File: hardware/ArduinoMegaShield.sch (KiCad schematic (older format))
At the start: 26 parts, among them SW101 SW_Coded, SW102 SW_Coded, SW103 SW_Coded, U101 A4988, U102 A4988, U103 A4988

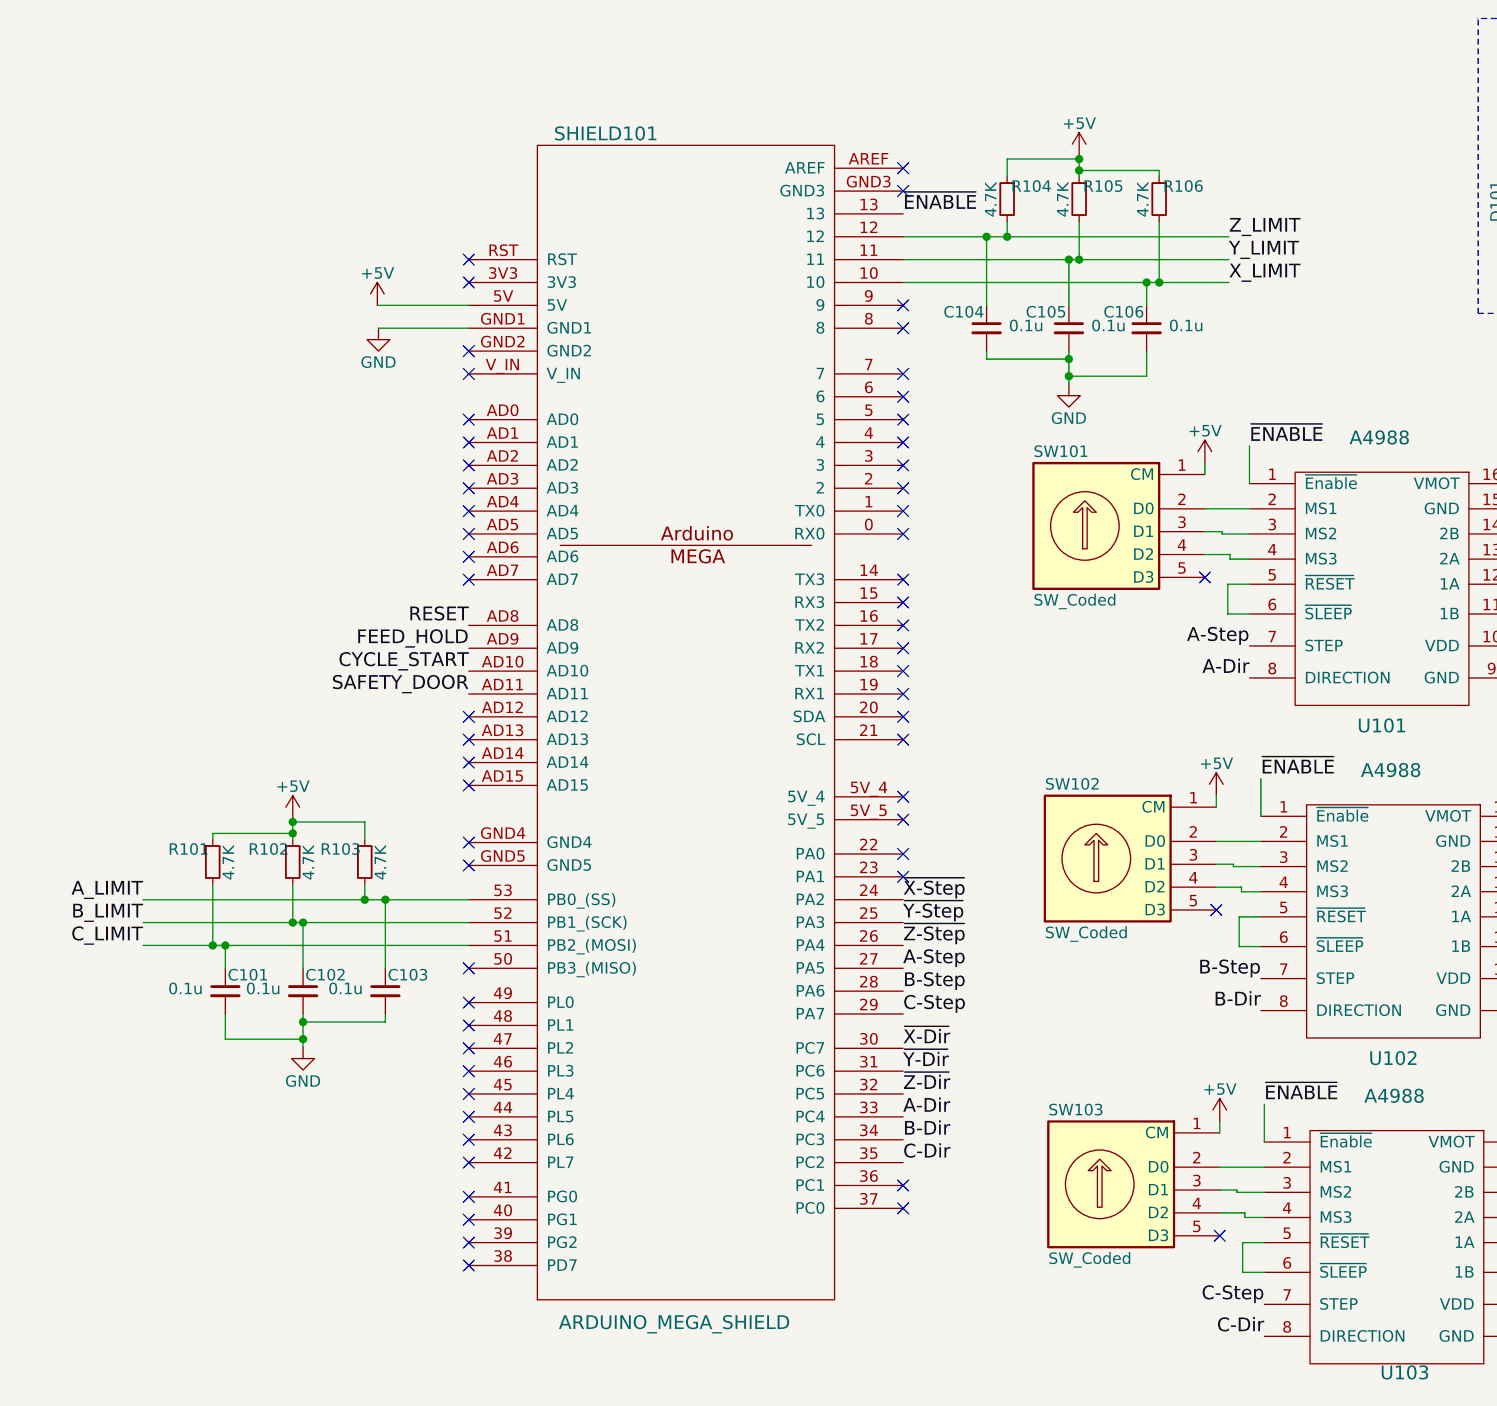
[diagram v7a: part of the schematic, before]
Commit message: changed connector footprints and added rotory dip switch footprint
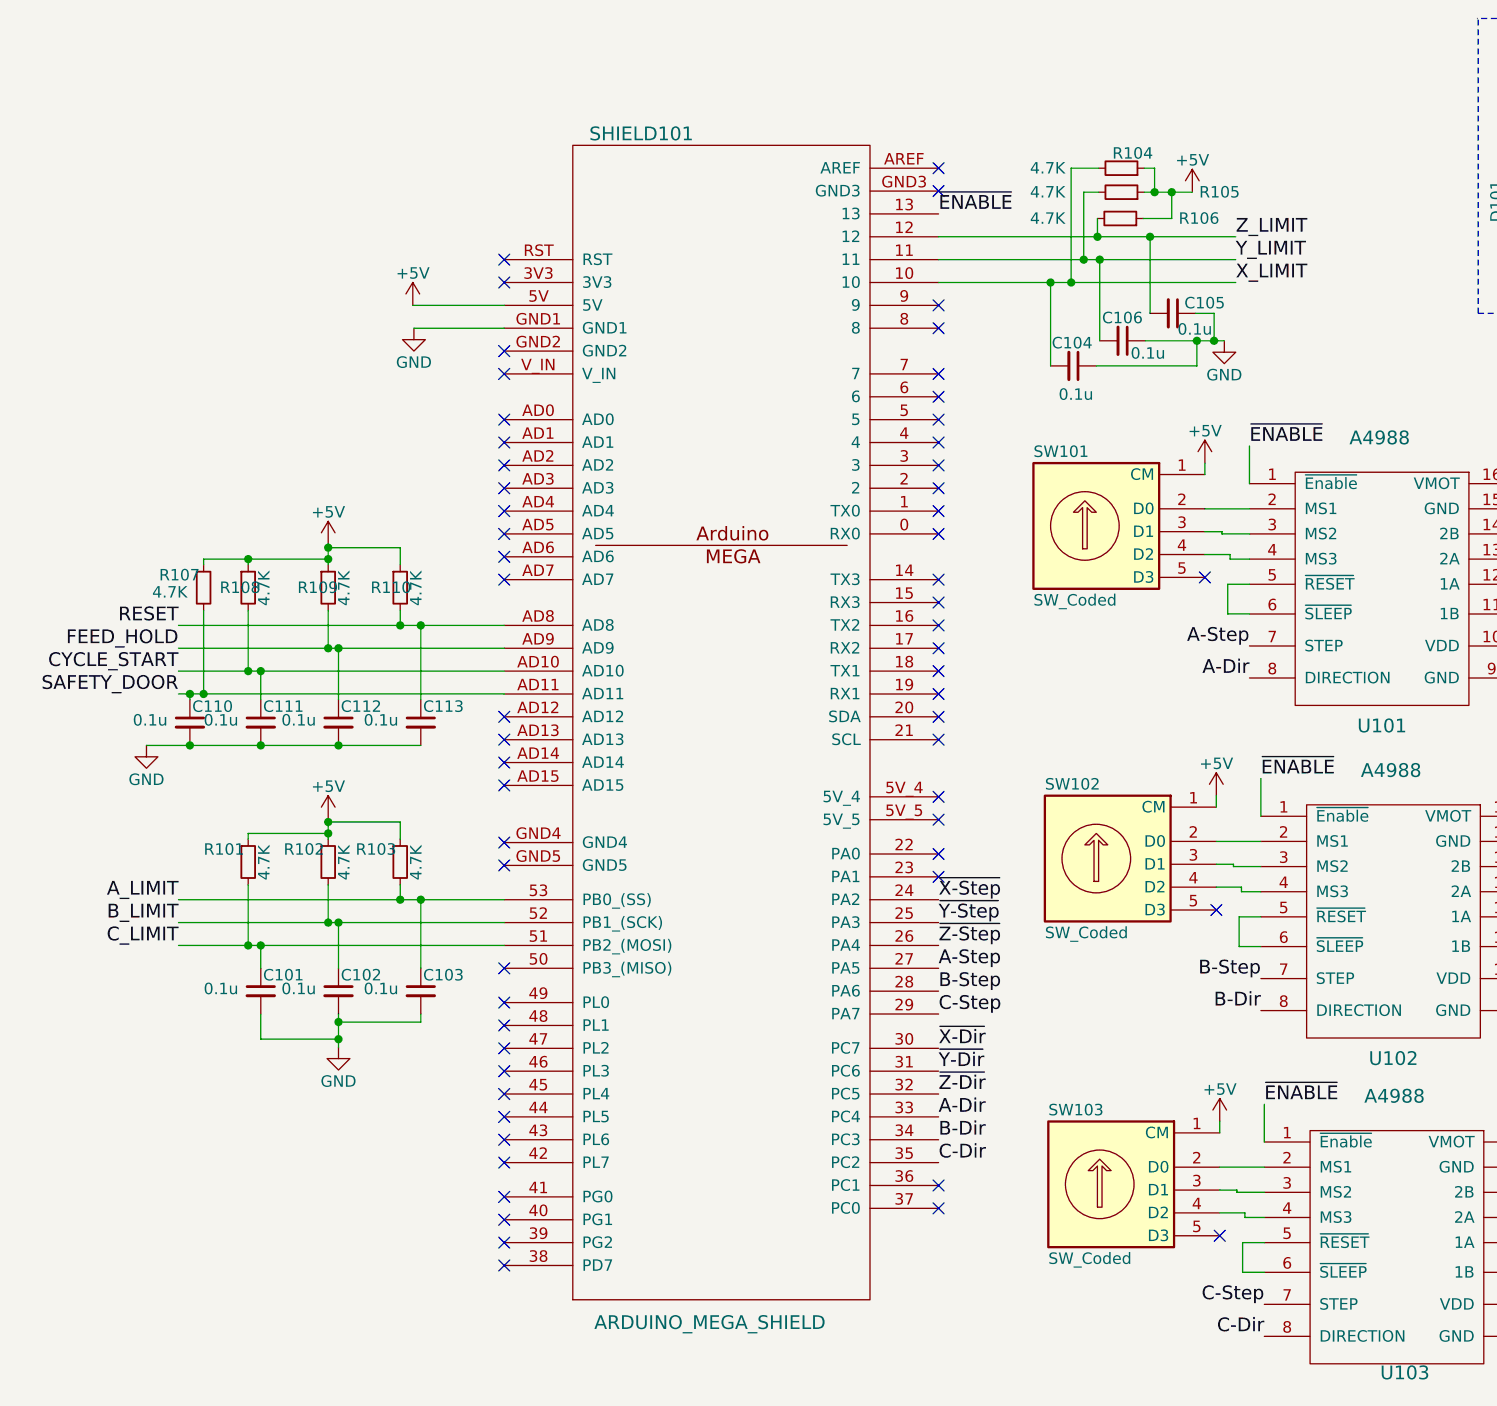
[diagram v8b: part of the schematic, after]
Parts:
- added C110, C111, C112, C113: 0.1u, Capacitors_SMD:C_0805_HandSoldering, symbol C_Small
- added R107, R108, R109, R110: 4.7K, Resistors_SMD:R_0805_HandSoldering, symbol R_Small
- SW101, SW102, SW103: footprint (none) -> 6axis:S-1010A
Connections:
- net +5V: now also R107.1, R108.1, R109.1, R110.1
- net CYCLE_START: now also C111.1, R108.2
- net FEED_HOLD: now also C112.1, R109.2
- net GND: now also C104.1, C105.1, C106.1, C110.2, C111.2, C112.2, C113.2; no longer C104.2, C105.2, C106.2
- net RESET: now also C113.1, R110.2
- net SAFETY_DOOR: now also C110.1, R107.2
- net X_LIMIT: now also C104.2, R104.2; no longer C106.1, R106.2
- net Y_LIMIT: now also C106.2; no longer C105.1
- net Z_LIMIT: now also C105.2, R106.2; no longer C104.1, R104.2
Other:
- moved on the sheet: C101, C102, C103, C104, C105, C106, R101, R102, R103, R104, R105, R106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
